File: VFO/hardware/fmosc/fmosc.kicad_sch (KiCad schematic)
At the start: 42 parts, among them J1 JST PH, J2 U.FL, J3 JST PH, J4 3670128, Q1 MMBT5179, Q2 MMBT5179, Q3 MMBT5179, Q4 MMBT5179

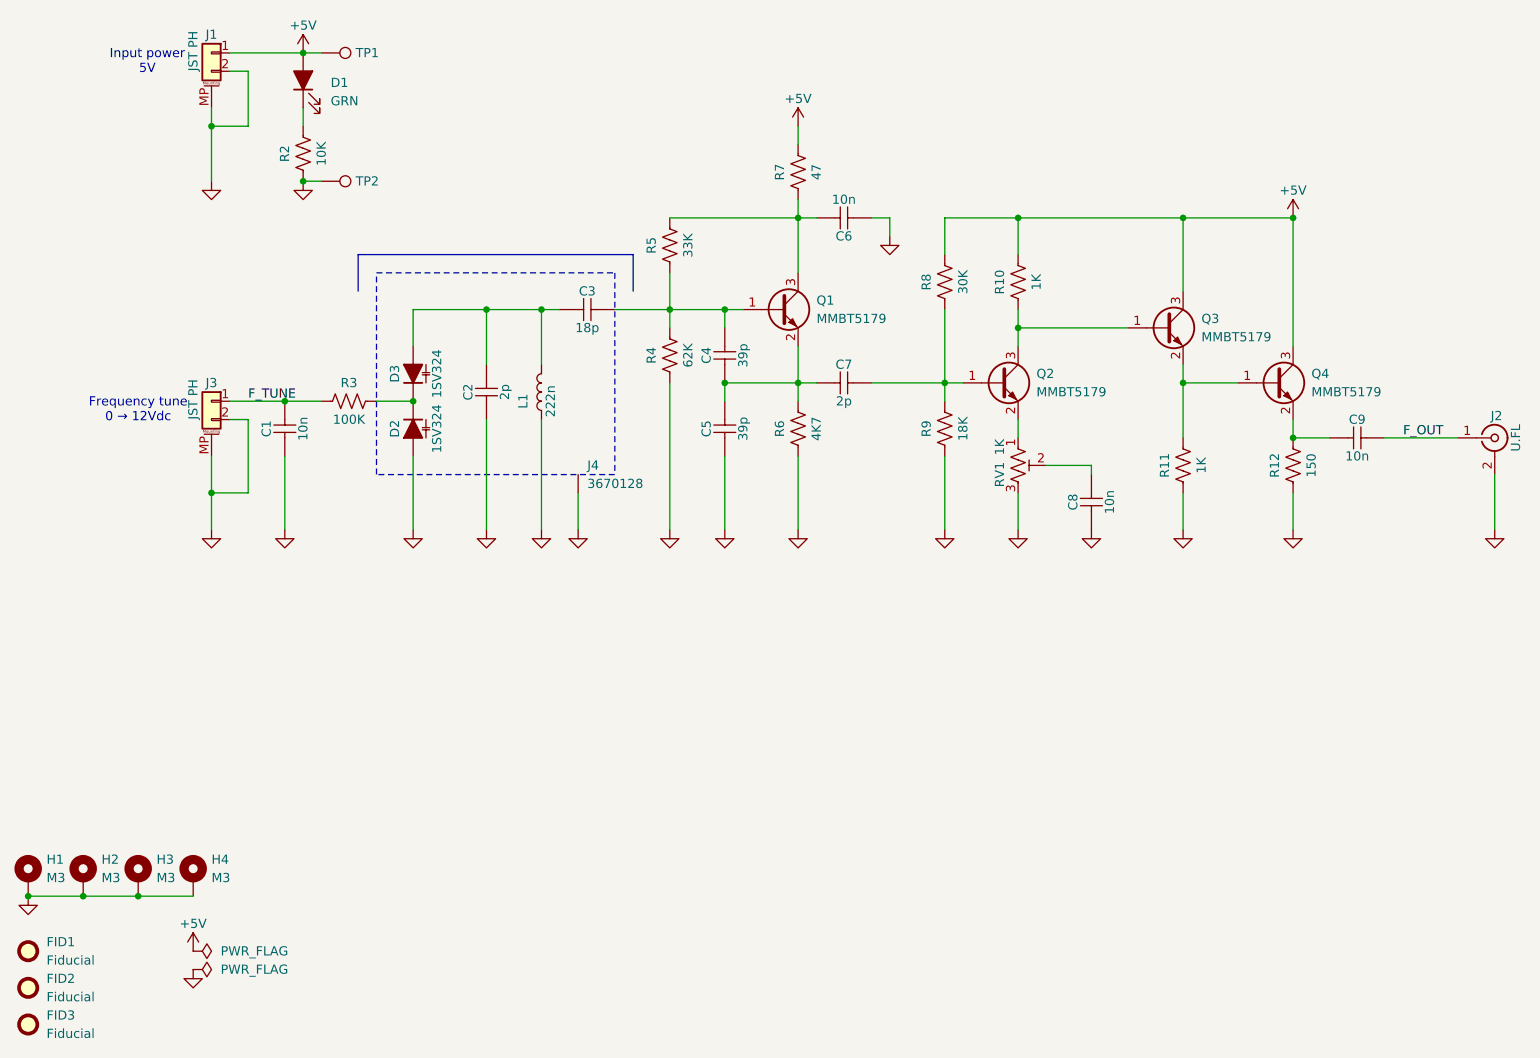
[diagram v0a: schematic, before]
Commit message: schematic ready for second version of the oscillator
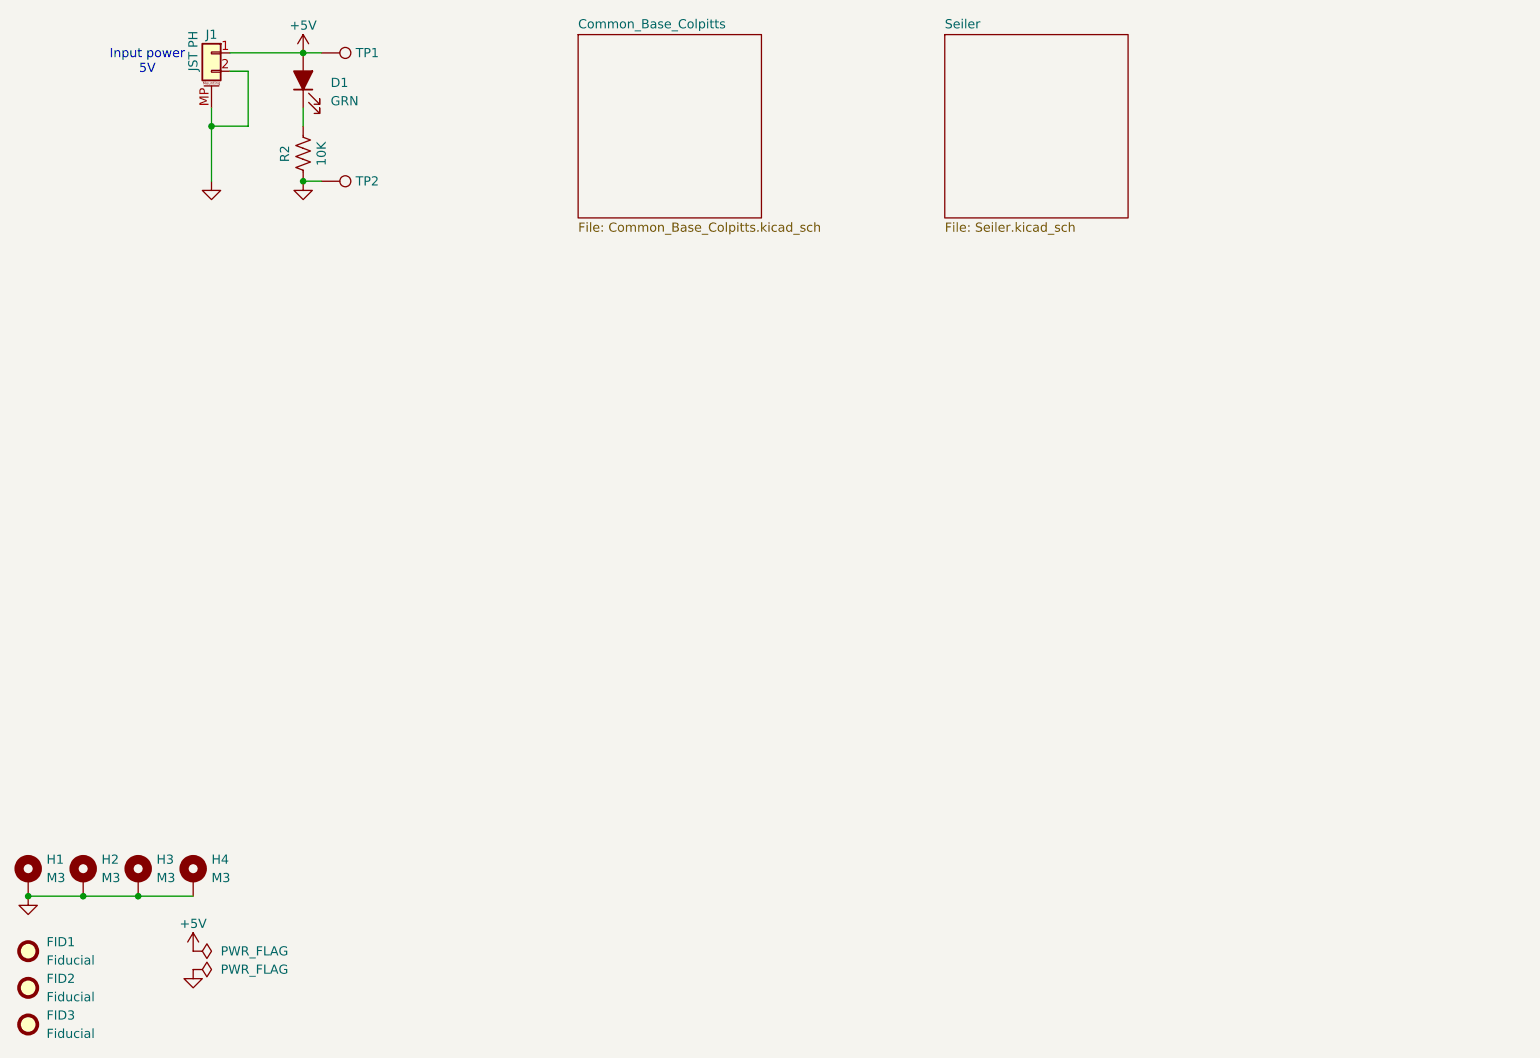
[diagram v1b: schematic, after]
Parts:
- removed C1, C6, C8, C9: 10n, g-cap:C_0603_1608Metric, symbol #gplm:cap/CAP-0000-0103
- removed C2, C7: 2p, g-cap:C_0603_1608Metric, symbol #gplm:cap/CAP-0000-02F0
- removed C3: 18p, g-cap:C_0603_1608Metric, symbol #gplm:cap/CAP-0000-0180
- removed C4, C5: 39p, g-cap:C_0603_1608Metric, symbol #gplm:cap/CAP-0000-0390
- removed D2, D3: 1SV324, g-dio:D_SOD-323, symbol #gplm:dio/DIO-0000-0000
- removed J2: U.FL, g-con:U.FL_Hirose_U.FL-R-SMT-1_Vertical, symbol #gplm:con/CON-0001-0000
- removed J3: JST PH, g-con:JST_PH_S2B-PH-SM4-TB_1x02-1MP_P2.00mm_Horizontal, symbol #gplm:con/CON-0000-0002
- removed J4: 3670128, g-rfm:H_Wurth_WE-SHC-SEAMLESS-FRAME_3670128, symbol #gplm:rfm/RFM-0000-0001
- removed L1: 222n, g-ind:L_Wurth_WE-CAIR-5910, symbol #gplm:ind/IND-0000-0221
- removed Q1, Q2, Q3, Q4: MMBT5179, g-SOT:SOT-23-3, symbol #gplm:trs/TRS-0000-0000
- removed R10, R11: 1K, g-res:R_0603_1608Metric, symbol #gplm:res/RES-0000-1001
- removed R12: 150, g-res:R_0603_1608Metric, symbol #gplm:res/RES-0000-1500
- removed R3: 100K, g-res:R_0603_1608Metric, symbol #gplm:res/RES-0000-1003
- removed R4: 62K, g-res:R_0603_1608Metric, symbol #gplm:res/RES-0000-6202
- removed R5: 33K, g-res:R_0603_1608Metric, symbol #gplm:res/RES-0000-3302
- removed R6: 4K7, g-res:R_0603_1608Metric, symbol #gplm:res/RES-0000-4701
- removed R7: 47, g-res:R_0603_1608Metric, symbol #gplm:res/RES-0000-0470
- removed R8: 30K, g-res:R_0603_1608Metric, symbol #gplm:res/RES-0000-3002
- removed R9: 18K, g-res:R_0603_1608Metric, symbol #gplm:res/RES-0000-1802
- removed RV1: 1K, g-rvr:Potentiometer_Bourns_3314J_Vertical, symbol #gplm:rvr/RVR-0000-1001
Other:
- added sheet Common_Base_Colpitts (Common_Base_Colpitts.kicad_sch)
- added sheet Seiler (Seiler.kicad_sch)
- note removed: "Frequency tune 0 → 12Vdc"

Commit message: release PBA-0000-0101
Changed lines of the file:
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@@
 		)
 		(instances
-			(project ""
+			(project "fmosc"
 				(path "/3dada041-f728-4295-8fb8-7b5173e4bef2"
 					(reference "#FLG01")
@@
 		)
 		(instances
-			(project ""
+			(project "fmosc"
 				(path "/3dada041-f728-4295-8fb8-7b5173e4bef2"
 					(reference "#FLG02")
@@
 		)
 		(instances
-			(project ""
+			(project "fmosc"
 				(path "/3dada041-f728-4295-8fb8-7b5173e4bef2"
 					(reference "TP1")
@@
 		)
 		(instances
-			(project ""
+			(project "fmosc"
 				(path "/3dada041-f728-4295-8fb8-7b5173e4bef2"
 					(reference "FID1")
@@
 		)
 		(instances
-			(project ""
+			(project "fmosc"
 				(path "/3dada041-f728-4295-8fb8-7b5173e4bef2"
 					(reference "TP2")
@@
 		)
 		(instances
-			(project "test1"
+			(project "fmosc"
 				(path "/3dada041-f728-4295-8fb8-7b5173e4bef2"
 					(reference "H2")
@@
 		)
 		(instances
-			(project ""
+			(project "fmosc"
 				(path "/3dada041-f728-4295-8fb8-7b5173e4bef2"
 					(reference "H1")
@@
 		)
 		(instances
-			(project "test1"
+			(project "fmosc"
 				(path "/3dada041-f728-4295-8fb8-7b5173e4bef2"
 					(reference "H3")
@@
 		)
 		(instances
-			(project "test1"
+			(project "fmosc"
 				(path "/3dada041-f728-4295-8fb8-7b5173e4bef2"
 					(reference "#PWR02")
@@
 		)
 		(instances
-			(project "test1"
+			(project "fmosc"
 				(path "/3dada041-f728-4295-8fb8-7b5173e4bef2"
 					(reference "#PWR021")
@@
 		)
 		(instances
-			(project "test1"
+			(project "fmosc"
 				(path "/3dada041-f728-4295-8fb8-7b5173e4bef2"
 					(reference "FID2")
@@
 		)
 		(instances
-			(project ""
+			(project "fmosc"
 				(path "/3dada041-f728-4295-8fb8-7b5173e4bef2"
 					(reference "D1")
@@
 		)
 		(instances
-			(project ""
+			(project "fmosc"
 				(path "/3dada041-f728-4295-8fb8-7b5173e4bef2"
 					(reference "R2")
@@
 		)
 		(instances
-			(project "test1"
+			(project "fmosc"
 				(path "/3dada041-f728-4295-8fb8-7b5173e4bef2"
 					(reference "FID3")
@@
 		)
 		(instances
-			(project ""
+			(project "fmosc"
 				(path "/3dada041-f728-4295-8fb8-7b5173e4bef2"
 					(reference "J1")
@@
 		)
 		(instances
-			(project "test1"
+			(project "fmosc"
 				(path "/3dada041-f728-4295-8fb8-7b5173e4bef2"
 					(reference "H4")
@@
 		)
 		(instances
-			(project ""
+			(project "fmosc"
 				(path "/3dada041-f728-4295-8fb8-7b5173e4bef2"
 					(reference "#PWR03")
@@
 		)
 		(instances
-			(project ""
+			(project "fmosc"
 				(path "/3dada041-f728-4295-8fb8-7b5173e4bef2"
 					(reference "#PWR01")
@@
 		(fields_autoplaced yes)
 		(stroke
-			(width 0.1524)
+			(width 0.3048)
 			(type solid)
 		)
 		(fill
-			(color 0 0 0 0.0000)
+			(color 0 255 0 1.0000)
 		)
 		(property "Sheetname" "Common_Base_Colpitts"
@@
 		(fields_autoplaced yes)
 		(stroke
-			(width 0.1524)
+			(width 0.3048)
 			(type solid)
 		)
 		(fill
-			(color 0 0 0 0.0000)
+			(color 0 255 0 1.0000)
 		)
 		(property "Sheetname" "Seiler"
